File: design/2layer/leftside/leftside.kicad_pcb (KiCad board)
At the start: 2 copper layers, 142.6 x 96.2 mm, 215 parts, among them IC1 XCL240B333FR-G, IC3 nRF52833-QDAA-R7, IC4 TCA9537DGSR, IC5 XCL110A503KR-G, IC6 TPS22917LDBVT, IC7 SN74AHCT1G125DCKR, J1 USB_C_Receptacle_USB2.0_16P, J2 Battery+, J3 Battery-, J4 OLED_128x32, J6 Conn_01x04, J7 F32Q-1A7H1-11012, U1 BQ27441-G1, U2 BQ24072RGT, U3 USB6B1, U5 PEC11L-4015F-S0015, U6 PEC11L-4015F-S0015, Y1 ECS-320-8-37B2-JTY-TR

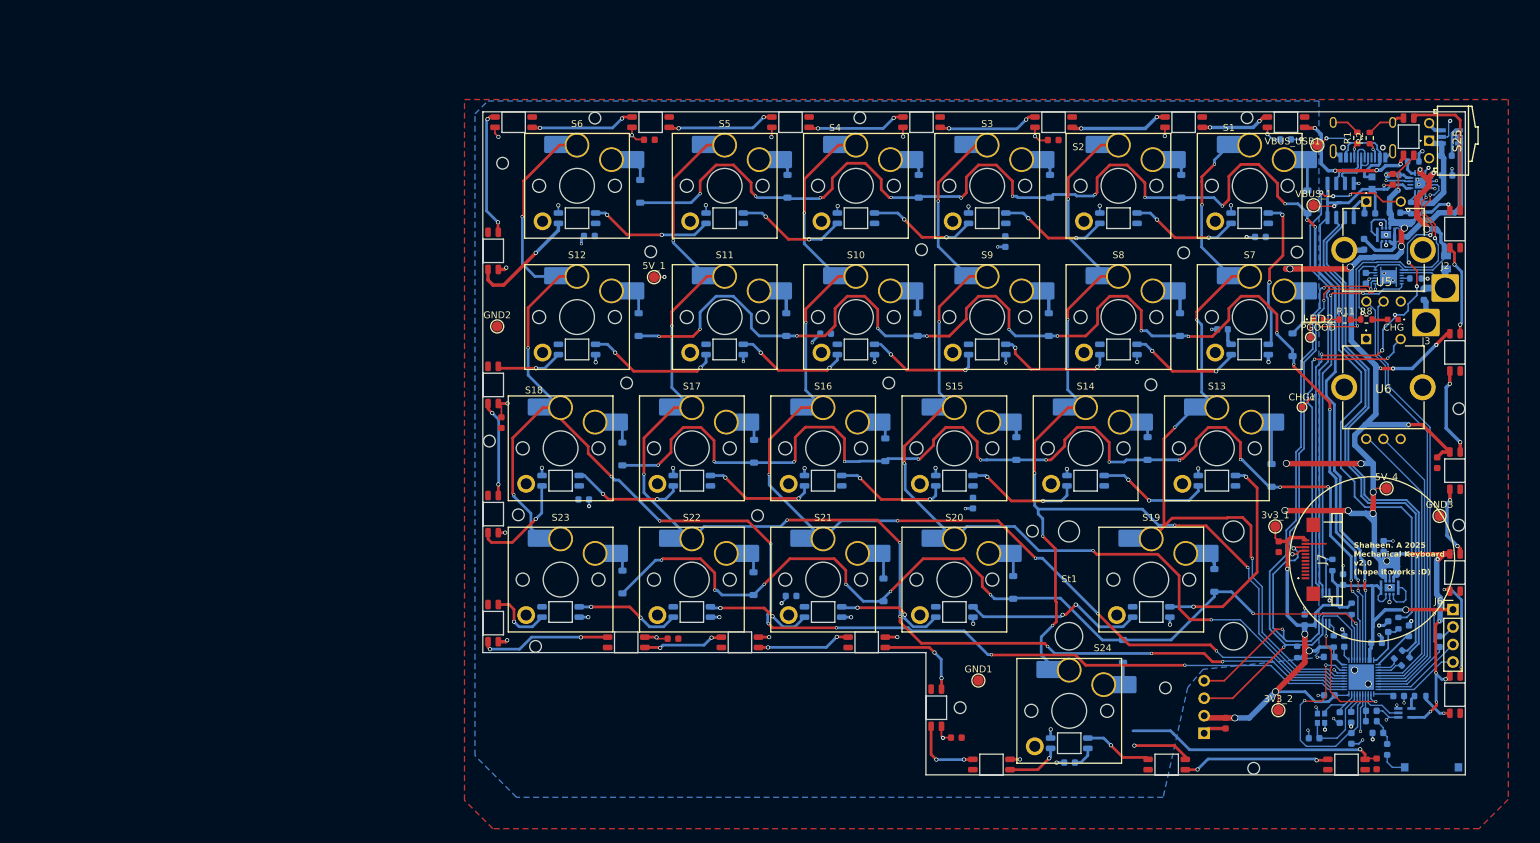
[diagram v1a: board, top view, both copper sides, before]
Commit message: begin better, more systematic 2 layer wiring
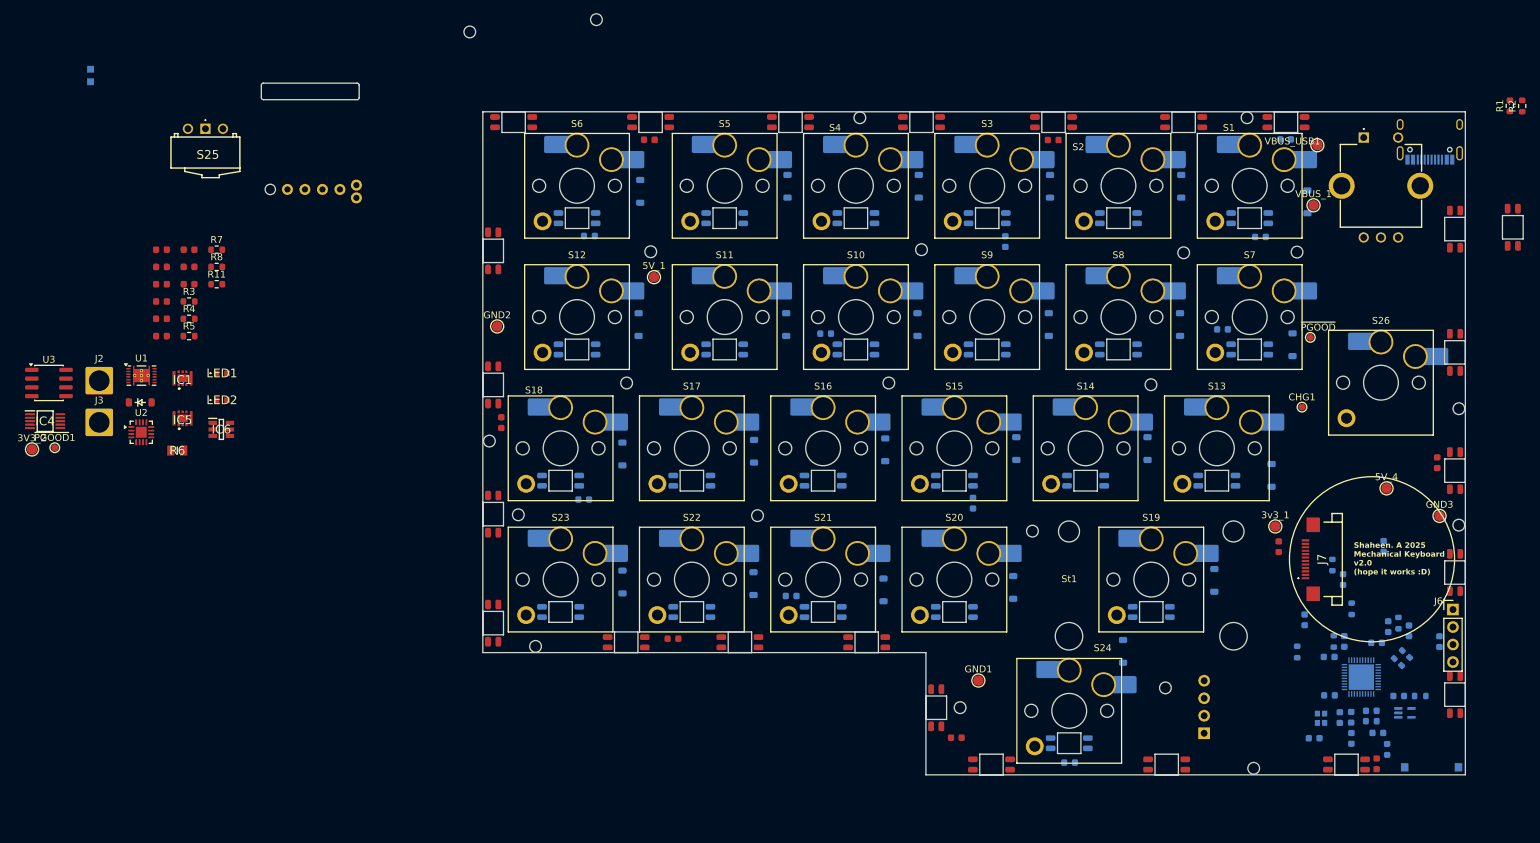
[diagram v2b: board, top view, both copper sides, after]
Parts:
- removed CHG: White LED KW_EEL, SamacSys_Parts:KWEELP41RUS1U13K6L3X4X5R18
- removed U6: PEC11L-4015F-S0015, SamacSys_Parts:PEC11L4015FS0015
- added Di25: Diode, ScottoKeebs_Components:Diode_SOD-123, F.Cu at (-31.7, 58.4)
- added EVQWGD1: ~, SamacSys_Parts:RollerEncoder_Panasonic_EVQWGD001, B.Cu at (-6.52, 21.9)
- added LED1: White LED KW_EEL, SamacSys:KWEELP41RUS1U13K6L3X4X5R18, F.Cu at (-19.8, 54.2)
- added S26: Keyswitch, ScottoKeebs_Hotswap:Hotswap_Choc_V1V2_Plated_1.00u, F.Cu at (148.4, 55.6)
- added ~{PGOOD}1: TestPoint, TestPoint:TestPoint_Pad_D1.0mm, F.Cu at (-44.1, 65.0)
- C10, C17, C22, C24, C25, C26, C48, R3, R4, R5, R7, U1, U2, U3: moved to F.Cu
- IC1, IC5: footprint SamacSys_Parts:XCL103D503CRG -> SamacSys:XCL103D503CRG; moved to F.Cu
- IC4: footprint SamacSys_Parts:SOP50P490X110-10N -> SamacSys:SOP50P490X110-10N; moved to F.Cu
- IC6: footprint SamacSys_Parts:SOT95P280X145-6N -> SamacSys:SOT95P280X145-6N; moved to F.Cu
- IC7: footprint SamacSys_Parts:SOT65P210X110-5N -> SamacSys:SOT65P210X110-5N
- J7: footprint SamacSys_Parts:F32Q1A7H111012 -> SamacSys:F32Q1A7H111012
- LED2: footprint SamacSys_Parts:KWEELP41RUS1U13K6L3X4X5R18 -> SamacSys:KWEELP41RUS1U13K6L3X4X5R18
- R6: footprint SamacSys_Parts:RESC2012X41N -> SamacSys:RESC2012X41N; moved to F.Cu
- Y1: footprint SamacSys_Parts:ECS320837B2JTYTR -> SamacSys:ECS320837B2JTYTR
- moved J2 195.8 mm to (-37.6, 55.3)
- moved J3 193.1 mm to (-37.6, 61.3)
- moved U3 189.3 mm to (-44.9, 55.6), turned to 0 degrees
- moved U2 189.1 mm to (-31.5, 62.8), turned to 0 degrees
- moved IC4 187.4 mm to (-45.5, 61.1), turned to 0 degrees
- moved C10 187.2 mm to (-28.6, 38.8)
- moved F1 186.6 mm to (-38.9, 11.0)
- moved R6 186.2 mm to (-26.3, 65.4), turned to 0 degrees
- moved 3V3_2 184.8 mm to (-47.4, 65.2)
- moved IC6 183.4 mm to (-19.9, 62.3)
- moved C48 183.3 mm to (-24.6, 41.3), turned to 0 degrees
- moved C17 183.2 mm to (-28.6, 41.3), turned to 0 degrees
- moved U1 181.6 mm to (-31.5, 54.5)
- moved C23 179.9 mm to (-28.6, 46.3), turned to 0 degrees
- moved R5 179.5 mm to (-24.6, 48.8), turned to 0 degrees
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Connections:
- Di1 pad 1: /Row 0 -> /Row 4
- Di11 pad 1: /Row 1 -> /Row 4
- Di20 pad 1: /Row 3 -> /Row 4
- Di4 pad 1: /Row 2 -> /Row 4
- IC3 pad 31: /Column 5 -> /Row 4
- S10 pad 1: /Column 3 -> /Column 2
- S11 pad 1: /Column 4 -> /Column 3
- S12 pad 1: /Column 5 -> /Column 4
- S13 pad 1: /Column 0 -> /Column 2
- S14 pad 1: /Column 1 -> /Column 0
- S15 pad 1: /Column 2 -> /Column 1
- S16 pad 1: /Column 3 -> /Column 2
- S17 pad 1: /Column 4 -> /Column 3
- S18 pad 1: /Column 5 -> /Column 4
- S19 pad 1: /Column 0 -> /Column 3
- S2 pad 1: /Column 1 -> /Column 0
- S20 pad 1: /Column 2 -> /Column 1
- S21 pad 1: /Column 3 -> /Column 2
- S22 pad 1: /Column 4 -> /Column 3
- S23 pad 1: /Column 5 -> /Column 4
- S24 pad 1: /Column 1 -> /Column 0
- S3 pad 1: /Column 2 -> /Column 1
- S4 pad 1: /Column 3 -> /Column 2
- S5 pad 1: /Column 4 -> /Column 3
- S6 pad 1: /Column 5 -> /Column 4
- S7 pad 1: /Column 0 -> /Column 1
- S8 pad 1: /Column 1 -> /Column 0
- S9 pad 1: /Column 2 -> /Column 1
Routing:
- net 5V: track 300.3 -> 0.00 mm, vias 43 -> 0
- net /Column 5: track 223.7 -> 0.00 mm, vias 10 -> 0
- net /Row 0: track 201.0 -> 0.00 mm, vias 14 -> 0
- net /Column 4: track 192.3 -> 0.00 mm, vias 9 -> 0
- net /Row 1: track 183.1 -> 0.00 mm, vias 14 -> 0
- net /Column 3: track 166.9 -> 0.00 mm, vias 7 -> 0
- net /Row 2: track 164.7 -> 0.00 mm, vias 14 -> 0
- net /Column 1: track 159.1 -> 0.00 mm, vias 7 -> 0
- net /Column 2: track 144.5 -> 0.00 mm, vias 5 -> 0
- net GND: track 138.7 -> 0.00 mm, vias 80 -> 0
- net /Row 3: track 137.3 -> 0.00 mm, vias 8 -> 0
- net 3V3: track 136.3 -> 0.00 mm, vias 7 -> 0
- net /Column 0: track 127.1 -> 0.00 mm, vias 5 -> 0
- net /SDA: track 102.3 -> 0.00 mm, vias 4 -> 0
- net /SCL: track 101.1 -> 0.00 mm, vias 4 -> 0
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- removed copper zone on B.Cu, net 5V
- removed copper zone on F.Cu, net GND
- removed copper zone on B.Cu, net Net-(IC5-1/VIN)
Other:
- board text added: "${REFERENCE}"

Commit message: V3 prep
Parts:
- removed the REF** at (117.1, 99.9)
- removed the REF** at (115.0, 55.9)
- removed the REF** at (38.9, 55.6)
- removed the REF** at (77.0, 55.6)
- removed the REF** at (23.2, 74.7)
- removed the REF** at (129.9, 111.5)
- removed the REF** at (119.8, 36.7)
- removed the REF** at (129.0, 17.1)
- removed the REF** at (159.7, 59.3)
- removed the REF** at (159.7, 76.2)
- removed the REF** at (19.0, 64.0)
- removed the REF** at (72.8, 17.1)
- removed the REF** at (57.9, 74.9)
- removed the REF** at (136.2, 36.6)
- removed the REF** at (81.7, 36.3)
- removed the REF** at (87.3, 102.7)
- removed the REF** at (16.1, 4.65)
- removed the REF** at (34.5, 2.87)
- removed the REF** at (25.7, 93.8)
- removed the REF** at (97.8, 77.1)
- removed ~{PGOOD}: TestPoint, TestPoint:TestPoint_Pad_D1.0mm
- added Di26: Diode, ScottoKeebs_Components:Diode_SOD-123, F.Cu at (-99.4, 68.4)
- added Di27: Diode, ScottoKeebs_Components:Diode_SOD-123, F.Cu at (-99.4, 71.8)
- added Di28: Diode, ScottoKeebs_Components:Diode_SOD-123, F.Cu at (-99.4, 75.1)
- added Di29: Diode, ScottoKeebs_Components:Diode_SOD-123, F.Cu at (-99.4, 78.5)
- added Di30: Diode, ScottoKeebs_Components:Diode_SOD-123, F.Cu at (-99.4, 81.8)
- added Di31: Diode, ScottoKeebs_Components:Diode_SOD-123, F.Cu at (-99.4, 85.2)
- added Di32: Diode, ScottoKeebs_Components:Diode_SOD-123, F.Cu at (-93.7, 68.4)
- added Di33: Diode, ScottoKeebs_Components:Diode_SOD-123, F.Cu at (-93.7, 71.8)
- added Di34: Diode, ScottoKeebs_Components:Diode_SOD-123, F.Cu at (-93.7, 75.1)
- added Di35: Diode, ScottoKeebs_Components:Diode_SOD-123, F.Cu at (-93.7, 78.5)
- added Di36: Diode, ScottoKeebs_Components:Diode_SOD-123, F.Cu at (-93.7, 81.8)
- added IC2: MCP23009-E_MG, LibraryLoader:QFN50P300X300X90-17N-D, F.Cu at (-88.2, 69.4)
- added IC8: TPS63051RMWT, LibraryLoader:QFN50P250X250X100-12N-D, F.Cu at (143.0, 97.4)
- added PC1: 10uF, ScottoKeebs_Components:Capacitor_0603, F.Cu at (-100.3, 42.9)
- added PC10: 100pF, ScottoKeebs_Components:Capacitor_0603, F.Cu at (-100.3, 57.9)
- added PC11: 100nF, ScottoKeebs_Components:Capacitor_0603, F.Cu at (-100.3, 60.5)
- added PC12: 1uF, ScottoKeebs_Components:Capacitor_0603, F.Cu at (-100.3, 63.0)
- added PC13: 1uF, ScottoKeebs_Components:Capacitor_0603, F.Cu at (-100.3, 65.5)
- added PC14: 47nF, ScottoKeebs_Components:Capacitor_0603, F.Cu at (-96.3, 42.9)
- added PC16: 4.7uF, ScottoKeebs_Components:Capacitor_0603, F.Cu at (-96.3, 45.4)
- added PC17: 4.7uF, ScottoKeebs_Components:Capacitor_0603, F.Cu at (-96.3, 47.9)
- added PC18: 100nF, ScottoKeebs_Components:Capacitor_0603, F.Cu at (-96.3, 50.4)
- added PC2: 4.7uF, ScottoKeebs_Components:Capacitor_0603, F.Cu at (-100.3, 45.4)
- added PC22: 470nF, ScottoKeebs_Components:Capacitor_0603, F.Cu at (-96.3, 52.9)
- added PC23: 4.7uF, ScottoKeebs_Components:Capacitor_0603, F.Cu at (-96.3, 55.4)
- added PC24: 4.7uF, ScottoKeebs_Components:Capacitor_0603, F.Cu at (-96.3, 57.9)
- added PC25: 10uF, ScottoKeebs_Components:Capacitor_0603, F.Cu at (-96.3, 60.5)
- added PC26: 10uF, ScottoKeebs_Components:Capacitor_0603, F.Cu at (-96.3, 63.0)
- added PC27: 10uF, ScottoKeebs_Components:Capacitor_0603, F.Cu at (-96.3, 65.5)
- added PC37: 100nF, ScottoKeebs_Components:Capacitor_0603, F.Cu at (-92.3, 42.9)
- added PC47: 10uF, ScottoKeebs_Components:Capacitor_0603, F.Cu at (-92.3, 45.4)
- added PC48: 4.7uF, ScottoKeebs_Components:Capacitor_0603, F.Cu at (-92.3, 47.9)
- added PC6: 4.7uF, ScottoKeebs_Components:Capacitor_0603, F.Cu at (-100.3, 47.9)
- added PC7: 100nF, ScottoKeebs_Components:Capacitor_0603, F.Cu at (-100.3, 50.4)
- added PC8: 820pF, ScottoKeebs_Components:Capacitor_0603, F.Cu at (-100.3, 52.9)
- added PC9: 4.7uF, ScottoKeebs_Components:Capacitor_0603, F.Cu at (-100.3, 55.4)
- added PG1: TestPoint, TestPoint:TestPoint_Pad_D1.5mm, F.Cu at (-84.2, 73.8)
- added PL3: 10uH, Inductor_SMD:L_0603_1608Metric, F.Cu at (-92.3, 50.4)
- added PL4: 15nH, Inductor_SMD:L_0603_1608Metric, F.Cu at (-92.3, 52.9)
- added PL5: 1.5uH, Inductor_SMD:L_0603_1608Metric, F.Cu at (-92.3, 55.4)
- added PR11: 270, Resistor_SMD:R_0603_1608Metric, F.Cu at (-92.3, 65.5)
- added PR17: 0, Resistor_SMD:R_0603_1608Metric, F.Cu at (-88.3, 42.9)
- added PR3: 1k8, Resistor_SMD:R_0603_1608Metric, F.Cu at (-92.3, 57.9)
- added PR4: 1k, Resistor_SMD:R_0603_1608Metric, F.Cu at (-92.3, 60.5)
- added PR8: 270, Resistor_SMD:R_0603_1608Metric, F.Cu at (-92.3, 63.0)
- added S27: Keyswitch, ScottoKeebs_Hotswap:Hotswap_Choc_V1V2_Plated_1.00u, F.Cu at (26.8, 24.4)
- added S28: Keyswitch, ScottoKeebs_Hotswap:Hotswap_Choc_V1V2_Plated_1.00u, F.Cu at (32.6, -57.2)
- added S29: Keyswitch, ScottoKeebs_Hotswap:Hotswap_Choc_V1V2_Plated_1.00u, F.Cu at (32.6, -39.9)
- added S30: Keyswitch, ScottoKeebs_Hotswap:Hotswap_Choc_V1V2_Plated_1.00u, F.Cu at (83.9, 24.4)
- added S31: Keyswitch, ScottoKeebs_Hotswap:Hotswap_Choc_V1V2_Plated_1.00u, F.Cu at (45.8, 24.4)
- added S32: Keyswitch, ScottoKeebs_Hotswap:Hotswap_Choc_V1V2_Plated_1.00u, F.Cu at (51.1, -57.2)
- added S33: Keyswitch, ScottoKeebs_Hotswap:Hotswap_Choc_V1V2_Plated_1.00u, F.Cu at (51.1, -39.9)
- added S34: Keyswitch, ScottoKeebs_Hotswap:Hotswap_Choc_V1V2_Plated_1.00u, F.Cu at (64.9, 24.4)
- added S35: Keyswitch, ScottoKeebs_Hotswap:Hotswap_Choc_V1V2_Plated_1.00u, F.Cu at (122.0, 24.4)
- added S36: Keyswitch, ScottoKeebs_Hotswap:Hotswap_Choc_V1V2_Plated_1.00u, F.Cu at (141.1, 24.4)
- added S37: Keyswitch, ScottoKeebs_Hotswap:Hotswap_Choc_V1V2_Plated_1.00u, F.Cu at (103.0, 24.4)
- added SC1: 12pF, ScottoKeebs_Components:Capacitor_0603, F.Cu at (-88.3, 45.4)
- added SC10: 10nF, ScottoKeebs_Components:Capacitor_0603, B.Cu at (144.1, 33.9)
- added SC19: 4.7uF, ScottoKeebs_Components:Capacitor_0603, F.Cu at (-88.3, 60.5)
- added SC2: 12pF, ScottoKeebs_Components:Capacitor_0603, F.Cu at (-88.3, 47.9)
- added SC3: 1pF, ScottoKeebs_Components:Capacitor_0603, F.Cu at (-88.3, 50.4)
- added SC4: 1.2pF, ScottoKeebs_Components:Capacitor_0603, F.Cu at (-88.3, 52.9)
- added SC5: 100nF, ScottoKeebs_Components:Capacitor_0603, F.Cu at (-88.3, 55.4)
- added SL1: 4.7nH, Inductor_SMD:L_0603_1608Metric, F.Cu at (-88.3, 63.0)
- added SL2: 2.2nH, Inductor_SMD:L_0603_1608Metric, F.Cu at (-88.3, 65.5)
- added SR1: 5k1, Resistor_SMD:R_0603_1608Metric, F.Cu at (-84.3, 42.9)
- added SR13: 4k7, Resistor_SMD:R_0603_1608Metric, F.Cu at (-84.3, 57.9)
- added SR14: 4k7, Resistor_SMD:R_0603_1608Metric, F.Cu at (-84.3, 60.5)
- added SR15: 22, Resistor_SMD:R_0603_1608Metric, F.Cu at (-84.3, 63.0)
- added SR16: 22, Resistor_SMD:R_0603_1608Metric, F.Cu at (-84.3, 65.5)
- added SR2: 5k1, Resistor_SMD:R_0603_1608Metric, F.Cu at (-84.3, 45.4)
- added SR3: 10k, Resistor_SMD:R_0603_1608Metric, F.Cu at (-84.3, 47.9)
- added SR4: 4k7, Resistor_SMD:R_0603_1608Metric, B.Cu at (147.1, 33.9)
- added SR5: 10k, Resistor_SMD:R_0603_1608Metric, F.Cu at (-84.3, 50.4)
- added SR7: 10k, Resistor_SMD:R_0603_1608Metric, F.Cu at (-84.3, 52.9)
- added SR9: 10k, Resistor_SMD:R_0603_1608Metric, F.Cu at (-84.3, 55.4)
- D15, D16, D17, D18, D19, D20, D21, D22, D23, D24, D25, D26, D29, D30, D31, D32, D33, D34, D35, D36, D37, D38, D39, D46, EVQWGD1, IC7, R10: moved to F.Cu
- IC6, R3, R4, R6, U2, U3: moved to B.Cu
- J2, J3: footprint Connector_Wire:SolderWire-2.5sqmm_1x01_D2.4mm_OD3.6mm -> Connector_Wire:SolderWire-0.75sqmm_1x01_D1.25mm_OD2.3mm
- moved GND3 226.9 mm to (-62.2, 15.6)
- moved 5V_4 221.9 mm to (-65.7, 15.6)
- moved 3v3_1 210.3 mm to (-69.3, 19.1)
- moved CHG1 209.1 mm to (-69.5, 26.0)
- moved U3 205.1 mm to (158.3, 27.5), turned to -90 degrees
- moved J3 202.7 mm to (162.9, 32.1)
- moved IC4 202.3 mm to (147.8, 120.6)
- moved VBUS_USB1 201.3 mm to (-62.2, 22.7)
- moved VBUS_1 201.0 mm to (-62.2, 19.1)
- moved IC5 198.9 mm to (171.5, 33.9)
- moved F1 193.3 mm to (153.9, 25.0)
- moved U1 187.2 mm to (154.4, 32.9), turned to 180 degrees
- moved C22 186.8 mm to (157.6, 29.5)
- moved LED2 184.8 mm to (162.5, 27.9), turned to 90 degrees
- moved U2 184.6 mm to (150.2, 30.3), turned to 180 degrees
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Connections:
- IC3 pad 14: /CCW2 -> /CW
- IC3 pad 15: /CW2 -> /CCW
- IC3 pad 16: /CCW -> /CCW2
- IC3 pad 17: /CW -> /LED
- IC3 pad 22: /INTA -> /CW2
- IC3 pad 23: /A -> /INTA
- IC3 pad 31: /Row 4 -> /Column 5
- IC3 pad 39: unconnected-(IC3-DCC-Pad39) -> Net-(IC3-DCC)
- IC3 pad 4: /Row 3 -> /CHG
- IC3 pad 5: /Row 2 -> /GPOUT
- IC3 pad 6: /Row 1 -> /NO
- IC3 pad 7: /Row 0 -> /NO2
- IC7 pad 2: /A -> /LED
- S25 pad 1: /OUT -> GND
- U1 pad 6: /BAT -> /SRP
- U2 pad 1: Net-(U2-TS) -> Net-(J5-Pin_1)
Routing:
- net Net-(IC6-ON): track 0.00 -> 118.4 mm
- net D-: track 0.00 -> 87.6 mm
- net D+: track 0.00 -> 87.5 mm
- net /SRP: track 0.00 -> 24.0 mm, vias 0 -> 1
- net Net-(IC3-SWDIO): track 0.00 -> 18.9 mm
- net /CCW: track 0.00 -> 18.4 mm, vias 0 -> 1
- net /CW: track 0.00 -> 18.4 mm, vias 0 -> 1
- net /CW2: track 0.00 -> 17.9 mm, vias 0 -> 1
- net Net-(IC3-SWDCLK): track 0.00 -> 17.1 mm
- net /~{PGOOD}: track 0.00 -> 15.7 mm, vias 0 -> 3
- net /CCW2: track 0.00 -> 15.6 mm, vias 0 -> 1
- net /BAT: track 0.00 -> 15.1 mm, vias 0 -> 2
- net Net-(D1-DOUT): track 0.00 -> 14.6 mm
- net /VBUS: track 0.00 -> 14.5 mm
- net /OUT: track 0.00 -> 8.67 mm
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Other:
- board size 142.6 x 96.2 mm -> 150 x 111.9 mm
- board text added: "Shaheen. A 2026 Mechanical Keyboard v3.0 (hope it works :D)"
- board text removed: "Shaheen. A 2025 Mechanical Keyboard v2.0 (hope it works :D)"

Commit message: Left side pre-stich
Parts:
- removed 3v3_1: TestPoint, TestPoint:TestPoint_Pad_D1.5mm
- removed C10: 100pF, ScottoKeebs_Components:Capacitor_0603
- removed C13, C25, C26: 10uF, ScottoKeebs_Components:Capacitor_0603
- removed C17, C23, C24, C47, C48, C9: 4.7uF, ScottoKeebs_Components:Capacitor_0603
- removed C18, C37, C7, C8: 100nF, ScottoKeebs_Components:Capacitor_0603
- removed C5: 1uF, ScottoKeebs_Components:Capacitor_0603
- removed Di31, Di32, Di33, Di35: Diode, ScottoKeebs_Components:Diode_SOD-123
- removed IC1: XCL240B333FR-G, SamacSys:XCL103D503CRG
- removed IC4: TCA9537DGSR, SamacSys:SOP50P490X110-10N
- removed the PC10 at (-100.3, 57.9)
- removed the PC13 at (-100.3, 65.5)
- removed the PC22 at (-96.3, 52.9)
- removed the PC8 at (-100.3, 52.9)
- removed the PR11 at (-92.3, 65.5)
- removed the PR3 at (-92.3, 57.9)
- removed the PR4 at (-92.3, 60.5)
- removed the PR8 at (-92.3, 63.0)
- removed R1, R2: 5k1, Resistor_SMD:R_0603_1608Metric
- removed R12, R5, R9: 10k, Resistor_SMD:R_0603_1608Metric
- removed R13, R14: 4k7, Resistor_SMD:R_0603_1608Metric
- removed R17: 0, Resistor_SMD:R_0603_1608Metric
- removed the S28 at (32.6, -57.2)
- removed the S29 at (32.6, -39.9)
- removed S32: Keyswitch, ScottoKeebs_Hotswap:Hotswap_Choc_V1V2_Plated_1.00u
- removed the S33 at (51.1, -39.9)
- removed the SC1 at (-88.3, 45.4)
- removed the SC2 at (-88.3, 47.9)
- removed the SC3 at (-88.3, 50.4)
- removed the SC4 at (-88.3, 52.9)
- removed the SL1 at (-88.3, 63.0)
- removed the SL2 at (-88.3, 65.5)
- removed the SR15 at (-84.3, 63.0)
- removed the SR16 at (-84.3, 65.5)
- removed the SR7 at (-84.3, 52.9)
- added D49: LED_SK6812MINI, ScottoKeebs_Components:LED_SK6812MINI, F.Cu at (148.2, 126.4)
- added D50: LED_SK6812MINI, ScottoKeebs_Components:LED_SK6812MINI, F.Cu at (133.3, 126.4)
- added D51: LED_SK6812MINI, ScottoKeebs_Components:LED_SK6812MINI, B.Cu at (83.9, 29.1)
- added D52: LED_SK6812MINI, ScottoKeebs_Components:LED_SK6812MINI, F.Cu at (74.4, 14.0)
- added D53: LED_SK6812MINI, ScottoKeebs_Components:LED_SK6812MINI, B.Cu at (131.6, 45.8)
- added D54: LED_SK6812MINI, ScottoKeebs_Components:LED_SK6812MINI, B.Cu at (131.6, 64.8)
- added D55: LED_SK6812MINI, ScottoKeebs_Components:LED_SK6812MINI, B.Cu at (126.8, 83.9)
- added D56: LED_SK6812MINI, ScottoKeebs_Components:LED_SK6812MINI, B.Cu at (117.3, 102.9)
- added D57: LED_SK6812MINI, ScottoKeebs_Components:LED_SK6812MINI, F.Cu at (119.0, 126.4)
- added D58: LED_SK6812MINI, ScottoKeebs_Components:LED_SK6812MINI, F.Cu at (100.6, 126.4)
- added D59: LED_SK6812MINI, ScottoKeebs_Components:LED_SK6812MINI, B.Cu at (79.2, 122.0)
- added D60: LED_SK6812MINI, ScottoKeebs_Components:LED_SK6812MINI, F.Cu at (86.3, 126.4)
- added D61: LED_SK6812MINI, ScottoKeebs_Components:LED_SK6812MINI, F.Cu at (55.4, 108.6)
- added D62: LED_SK6812MINI, ScottoKeebs_Components:LED_SK6812MINI, F.Cu at (68.8, 116.0)
- added D63: LED_SK6812MINI, ScottoKeebs_Components:LED_SK6812MINI, F.Cu at (72.0, 126.4)
- added J5: Conn_01x01, TestPoint:TestPoint_Pad_1.0x1.0mm, B.Cu at (155.6, 36.6)
- added J8: Conn_01x01, TestPoint:TestPoint_Pad_1.0x1.0mm, B.Cu at (154.9, 39.6)
- added PC3: 10uF, ScottoKeebs_Components:Capacitor_0603, B.Cu at (139.0, 95.1)
- C1, C2, C4: value 4.7uF -> 100nF
- C29, C30, C34, C38, C39, C41, C45, D13, D15, D17, D19, D21, D23, D26, D27, D28, D29, D30, D31, D32, D33, D34, D35, D38, D39, D4, D40, D41, D42, D43, D44, D45, D46, IC2, IC5, IC7, IC8, PC1, PC11, PC14, PC16, PC18, PC23, PC25, PC26, PC27, PC37, PC47, PC48, PC6, PC7, PC9, PL3, PL4, PL5, PR17, SC19, SC5, SR13, SR14, SR3, SR5, SR9, U1: moved to B.Cu
- Di1, Di10, Di11, Di12, Di13, Di14, Di15, Di16, Di17, Di18, Di19, Di2, Di20, Di21, Di22, Di23, Di24, Di3, Di4, Di5, Di6, Di7, Di8, Di9: moved to F.Cu
- PC22: renamed from C22; moved to B.Cu
- PR3: renamed from R3; value 540 -> 1k8
- PR4: renamed from R4; value 590 -> 1k
- SR10: renamed from R10; moved to B.Cu
- SR7: renamed from R7; moved to B.Cu
- VBUS_1, VBUS_USB1: footprint TestPoint:TestPoint_Pad_D1.5mm -> TestPoint:TestPoint_Pad_D1.0mm
- moved PC7 268.4 mm to (160.6, 113.7), turned to 45 degrees
- moved PC6 261.6 mm to (154.2, 108.7), turned to -135 degrees
- moved PC16 261.2 mm to (158.2, 104.2)
- moved PC24 255.2 mm to (156.4, 22.4), turned to 90 degrees
- moved Di36 254.0 mm to (153.0, 21.0), turned to 180 degrees
- moved Di34 253.5 mm to (159.3, 59.4), turned to -90 degrees
- moved PC2 252.7 mm to (151.9, 30.1), turned to -90 degrees
- moved PR17 252.1 mm to (156.7, 102.7)
- moved PC17 251.2 mm to (154.3, 30.1), turned to 180 degrees
- moved PC14 250.8 mm to (142.4, 119.7), turned to 180 degrees
- moved PC1 250.7 mm to (143.5, 101.3), turned to 90 degrees
- moved PC12 249.5 mm to (144.4, 111.6)
- moved SC19 249.2 mm to (156.0, 109.6), turned to -135 degrees
- moved PC23 247.6 mm to (149.3, 24.3)
- moved PC11 246.5 mm to (139.2, 118.5), turned to -90 degrees
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- renumbered C12 to PC10, C6 to PC13, C11 to PC8, R11 to PR11, R8 to PR8, S25 to S0, S23 to S1, S31 to S10, S21 to S11, S16 to S12, S10 to S13, S4 to S14, S34 to S15, S20 to S16, S15 to S17, S9 to S18, S3 to S19, S18 to S2, S30 to S20, S24 to S21, S14 to S22, S8 to S23, S2 to S24, S37 to S25, S19 to S26, S13 to S27, S7 to S28, S1 to S29, S12 to S3, S35 to S30, S26 to S33, S36 to S35, S6 to S4, S27 to S5, S22 to S6, S17 to S7, S11 to S8, S5 to S9, C14 to SC1, C19 to SC2, C16 to SC3, C15 to SC4, L1 to SL1, L2 to SL2, R15 to SR15, R16 to SR16
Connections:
- C1 pad 1: GND -> 5V
- C1 pad 2: 3V3 -> GND
- C2 pad 1: GND -> 5V
- C2 pad 2: Net-(IC3-VBUS) -> GND
- C3 pad 1: GND -> 5V
- C3 pad 2: Net-(IC3-DEC1) -> GND
- C4 pad 1: GND -> 5V
- C4 pad 2: Net-(IC3-DECUSB) -> GND
- D1 pad 2: Net-(D1-DOUT) -> unconnected-(D1-DOUT-Pad2)
- D11 pad 4: Net-(D10-DOUT) -> Net-(D11-DIN)
- D12 pad 2: Net-(D12-DOUT) -> Net-(D11-DIN)
- D12 pad 4: Net-(D11-DOUT) -> Net-(D12-DIN)
- D13 pad 2: Net-(D13-DOUT) -> Net-(D12-DIN)
- D13 pad 4: Net-(D12-DOUT) -> Net-(D13-DIN)
- D14 pad 2: Net-(D14-DOUT) -> Net-(D13-DIN)
- D14 pad 4: Net-(D13-DOUT) -> Net-(D14-DIN)
- D15 pad 2: Net-(D15-DOUT) -> Net-(D14-DIN)
- D15 pad 4: Net-(D14-DOUT) -> Net-(D15-DIN)
- D16 pad 2: Net-(D16-DOUT) -> Net-(D15-DIN)
- D16 pad 4: Net-(D15-DOUT) -> Net-(D16-DIN)
- D17 pad 2: Net-(D17-DOUT) -> Net-(D16-DIN)
- D17 pad 4: Net-(D16-DOUT) -> Net-(D17-DIN)
- D18 pad 2: Net-(D18-DOUT) -> Net-(D17-DIN)
- D18 pad 4: Net-(D17-DOUT) -> Net-(D18-DIN)
- D19 pad 4: Net-(D18-DOUT) -> Net-(D19-DIN)
- D2 pad 2: Net-(D2-DOUT) -> Net-(D1-DIN)
- D2 pad 4: Net-(D1-DOUT) -> Net-(D2-DIN)
- D20 pad 2: Net-(D20-DOUT) -> Net-(D19-DIN)
- D20 pad 4: Net-(D19-DOUT) -> Net-(D20-DIN)
- D21 pad 2: Net-(D21-DOUT) -> Net-(D20-DIN)
- D21 pad 4: Net-(D20-DOUT) -> Net-(D21-DIN)
- D22 pad 2: Net-(D22-DOUT) -> Net-(D21-DIN)
- D22 pad 4: Net-(D21-DOUT) -> Net-(D22-DIN)
- D23 pad 4: Net-(D22-DOUT) -> Net-(D23-DIN)
- D24 pad 2: Net-(D24-DOUT) -> Net-(D22-DIN)
- D24 pad 4: Net-(D23-DOUT) -> Net-(D24-DIN)
- D25 pad 2: Net-(D25-DOUT) -> Net-(D24-DIN)
- D25 pad 4: Net-(D24-DOUT) -> Net-(D23-DOUT)
- D26 pad 4: Net-(D25-DOUT) -> Net-(D26-DIN)
- D27 pad 2: Net-(D27-DOUT) -> Net-(D26-DIN)
- D27 pad 4: Net-(D26-DOUT) -> Net-(D27-DIN)
- D28 pad 2: Net-(D28-DOUT) -> Net-(D27-DIN)
- D28 pad 4: Net-(D27-DOUT) -> Net-(D28-DIN)
- D29 pad 2: Net-(D29-DOUT) -> Net-(D28-DIN)
- D29 pad 4: Net-(D28-DOUT) -> Net-(D29-DIN)
- D3 pad 2: Net-(D3-DOUT) -> Net-(D2-DIN)
- D3 pad 4: Net-(D2-DOUT) -> Net-(D3-DIN)
- D30 pad 2: Net-(D30-DOUT) -> Net-(D29-DIN)
- D30 pad 4: Net-(D29-DOUT) -> Net-(D30-DIN)
- D31 pad 4: Net-(D30-DOUT) -> Net-(D31-DIN)
- D32 pad 2: Net-(D32-DOUT) -> Net-(D31-DIN)
- D32 pad 4: Net-(D31-DOUT) -> Net-(D32-DIN)
- D33 pad 2: Net-(D33-DOUT) -> Net-(D32-DIN)
- D33 pad 4: Net-(D32-DOUT) -> Net-(D33-DIN)
- D34 pad 2: Net-(D34-DOUT) -> Net-(D33-DIN)
- D34 pad 4: Net-(D33-DOUT) -> Net-(D34-DIN)
- D35 pad 2: Net-(D35-DOUT) -> Net-(D34-DIN)
- D35 pad 4: Net-(D34-DOUT) -> Net-(D35-DIN)
- D36 pad 2: Net-(D36-DOUT) -> Net-(D35-DIN)
- D36 pad 4: Net-(D35-DOUT) -> Net-(D36-DIN)
- D37 pad 2: Net-(D37-DOUT) -> Net-(D36-DIN)
- D37 pad 4: Net-(D36-DOUT) -> Net-(D37-DIN)
- D38 pad 2: Net-(D38-DOUT) -> Net-(D37-DIN)
- D38 pad 4: Net-(D37-DOUT) -> Net-(D38-DIN)
- D39 pad 2: Net-(D39-DOUT) -> Net-(D38-DIN)
- D39 pad 4: Net-(D38-DOUT) -> Net-(D39-DIN)
- D4 pad 2: Net-(D4-DOUT) -> Net-(D3-DIN)
- D4 pad 4: Net-(D3-DOUT) -> Net-(D4-DIN)
- D40 pad 2: Net-(D40-DOUT) -> Net-(D39-DIN)
- D40 pad 4: Net-(D39-DOUT) -> Net-(D40-DIN)
- D41 pad 2: Net-(D41-DOUT) -> Net-(D40-DIN)
- D41 pad 4: Net-(D40-DOUT) -> Net-(D41-DIN)
- D42 pad 2: Net-(D42-DOUT) -> Net-(D41-DIN)
- D42 pad 4: Net-(D41-DOUT) -> Net-(D42-DIN)
- D43 pad 4: Net-(D42-DOUT) -> Net-(D43-DIN)
- D44 pad 2: Net-(D44-DOUT) -> Net-(D43-DIN)
- D44 pad 4: Net-(D43-DOUT) -> Net-(D44-DIN)
- D45 pad 2: Net-(D45-DOUT) -> Net-(D44-DIN)
- D45 pad 4: Net-(D44-DOUT) -> Net-(D45-DIN)
- D46 pad 2: Net-(D46-DOUT) -> Net-(D45-DIN)
- D46 pad 4: Net-(D45-DOUT) -> Net-(D10-DOUT)
- D47 pad 2: Net-(D47-DOUT) -> Net-(D23-DIN)
- D47 pad 4: Net-(D46-DOUT) -> Net-(D26-DOUT)
- D48 pad 2: unconnected-(D48-DOUT-Pad2) -> Net-(D4-DIN)
- D48 pad 4: Net-(D47-DOUT) -> Net-(D48-DIN)
- D5 pad 2: Net-(D5-DOUT) -> Net-(D48-DIN)
- D5 pad 4: Net-(D4-DOUT) -> Net-(D5-DIN)
- D6 pad 2: Net-(D6-DOUT) -> Net-(D5-DIN)
- D6 pad 4: Net-(D5-DOUT) -> Net-(D6-DIN)
- D7 pad 2: Net-(D7-DOUT) -> Net-(D6-DIN)
- D7 pad 4: Net-(D6-DOUT) -> Net-(D11-DOUT)
- D8 pad 2: Net-(D8-DOUT) -> Net-(D10-DIN)
- D8 pad 4: Net-(D7-DOUT) -> Net-(D8-DIN)
- D9 pad 2: Net-(D10-DIN) -> Net-(D8-DIN)
- D9 pad 4: Net-(D8-DOUT) -> Net-(D61-DOUT)
- Di1 pad 1: /Row 4 -> /Row 0
- Di10 pad 1: /Row 0 -> /Row 1
- Di11 pad 1: /Row 4 -> /Row 5
- Di12 pad 1: /Row 1 -> /Row 0
- Di13 pad 1: /Row 1 -> /Row 2
- Di14 pad 1: /Row 1 -> /Row 2
- Di15 pad 1: /Row 1 -> /Row 2
- Di16 pad 1: /Row 2 -> /Row 0
- Di17 pad 1: /Row 2 -> /Row 4
- Di18 pad 1: /Row 2 -> /Row 3
- Di19 pad 1: /Row 2 -> /Row 3
- Di2 pad 1: /Row 0 -> /Row 1
- Di20 pad 1: /Row 4 -> /Row 5
- Di22 pad 1: /Row 3 -> /Row 4
- Di23 pad 1: /Row 3 -> /Row 4
- Di24 pad 1: /Row 3 -> /Row 0
- Di25 pad 1: /Row 4 -> /Row 5
- Di26 pad 1: /Row 0 -> /Row 1
- Di27 pad 1: /Row 1 -> /Row 2
- Di28 pad 1: /Row 2 -> /Row 3
- Di29 pad 1: /Row 3 -> /Row 4
- Di3 pad 1: /Row 1 -> /Row 2
- Di30 pad 1: /Row 4 -> /Row 5
- Di34 pad 1: /Row 5 -> /Row 6
- Di36 pad 1: /Row 5 -> /Row 6
- Di4 pad 1: /Row 4 -> /Row 5
- Di5 pad 1: /Row 2 -> /Row 3
- Di6 pad 1: /Row 3 -> /Row 4
- Di8 pad 1: /Row 0 -> /Row 1
- Di9 pad 1: /Row 0 -> /Row 1
- IC2 pad 10: /Row 1 -> /Row 5
- IC2 pad 11: /Row 2 -> /Row 6
- IC2 pad 12: /Row 3 -> /Row 0
- IC2 pad 13: /Row 4 -> /Row 1
- IC2 pad 14: /Row 5 -> /Row 2
- IC2 pad 15: unconnected-(IC2-GP6-Pad15) -> /Row 3
- IC2 pad 16: unconnected-(IC2-GP7-Pad16) -> /Row 4
- IC2 pad 9: /Row 0 -> unconnected-(IC2-GP0-Pad9)
- IC3 pad 14: /CW -> /CCW
- IC3 pad 15: /CCW -> /CW
- IC3 pad 17: /LED -> /Column 2
- IC3 pad 23: /INTA -> unconnected-(IC3-P0.10-Pad23)
- IC3 pad 31: /Column 5 -> /LED
- IC3 pad 32: /Column 4 -> /INTA
- IC3 pad 33: /Column 3 -> /Column 0
- IC3 pad 34: /Column 2 -> /Column 3
- IC3 pad 36: /Column 0 -> /Column 4
- IC3 pad 4: /CHG -> /GPOUT
- IC3 pad 5: /GPOUT -> /NO2
- IC3 pad 6: /NO -> /CHG
- IC3 pad 7: /NO2 -> /NO
- S1 pad 1: /Column 4 -> /Column 0
- S1 pad 2: Net-(Di23-A) -> Net-(Di1-A)
- S10 pad 1: /Column 5 -> /Column 4
- S10 pad 2: Net-(Di30-A) -> Net-(Di26-A)
- S11 pad 1: /Column 2 -> /Column 0
- S11 pad 2: Net-(Di6-A) -> Net-(Di3-A)
- S12 pad 1: /Column 2 -> /Column 1
- S12 pad 2: Net-(Di18-A) -> Net-(Di13-A)
- S13 pad 2: Net-(Di13-A) -> Net-(Di14-A)
- S14 pad 1: /Column 2 -> /Column 3
- S14 pad 2: Net-(Di9-A) -> Net-(Di15-A)
- S15 pad 1: /Column 2 -> /Column 4
- S15 pad 2: Net-(Di33-A) -> Net-(Di27-A)
- S16 pad 1: /Column 1 -> /Column 0
- S17 pad 2: Net-(Di17-A) -> Net-(Di18-A)
- S18 pad 1: /Column 1 -> /Column 2
- S18 pad 2: Net-(Di3-A) -> Net-(Di5-A)
- S19 pad 1: /Column 1 -> /Column 3
- S19 pad 2: Net-(Di8-A) -> Net-(Di19-A)
- S2 pad 1: /Column 4 -> /Column 1
- S2 pad 2: Net-(Di19-A) -> Net-(Di7-A)
- S20 pad 1: /Column 5 -> /Column 4
- S20 pad 2: Net-(Di29-A) -> Net-(Di28-A)
- S21 pad 2: Net-(Di24-A) -> Net-(Di17-A)
- S22 pad 1: /Column 0 -> /Column 1
- S22 pad 2: Net-(Di16-A) -> Net-(Di6-A)
- S23 pad 1: /Column 0 -> /Column 2
- S23 pad 2: Net-(Di12-A) -> Net-(Di22-A)
- S24 pad 1: /Column 0 -> /Column 3
- S24 pad 2: Net-(Di7-A) -> Net-(Di23-A)
- S25 pad 1: /Column 5 -> /Column 4
- S25 pad 2: Net-(Di36-A) -> Net-(Di29-A)
- S26 pad 1: /Column 3 -> /Column 0
- S26 pad 2: Net-(Di20-A) -> Net-(Di11-A)
- S27 pad 1: /Column 2 -> /Column 1
- S28 pad 1: /Column 1 -> /Column 2
- S28 pad 2: Net-(Di11-A) -> Net-(Di20-A)
- S29 pad 1: /Column 0 -> /Column 3
- S29 pad 2: Net-(Di1-A) -> Net-(Di25-A)
- S3 pad 1: /Column 4 -> /Column 2
- S3 pad 2: Net-(Di15-A) -> Net-(Di12-A)
- S30 pad 1: /Column 3 -> /Column 4
- S30 pad 2: Net-(Di34-A) -> Net-(Di30-A)
- S33 pad 1: /Column 4 -> /Column 2
- S33 pad 2: Net-(Di25-A) -> Net-(Di34-A)
- S35 pad 2: Net-(Di35-A) -> Net-(Di36-A)
- S4 pad 1: /Column 4 -> /Column 3
- S4 pad 2: Net-(Di10-A) -> Net-(Di16-A)
- S5 pad 1: /Column 5 -> /Column 4
- S5 pad 2: Net-(Di26-A) -> Net-(Di24-A)
- S6 pad 1: /Column 3 -> /Column 0
- S6 pad 2: Net-(Di22-A) -> Net-(Di8-A)
- S7 pad 1: /Column 3 -> /Column 1
- S7 pad 2: Net-(Di5-A) -> Net-(Di9-A)
- S8 pad 1: /Column 3 -> /Column 2
- S8 pad 2: Net-(Di14-A) -> Net-(Di2-A)
- S9 pad 2: Net-(Di2-A) -> Net-(Di10-A)
- SR10 pad 2: Net-(D1-DIN) -> Net-(D49-DIN)
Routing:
- net /Column 4: track 0.00 -> 252.1 mm, vias 0 -> 16
- net /Column 3: track 0.00 -> 217.3 mm, vias 0 -> 10
- net /Column 2: track 0.00 -> 204.2 mm, vias 0 -> 5
- net /Row 0: track 0.00 -> 196.6 mm, vias 0 -> 17
- net /Row 1: track 0.00 -> 183.2 mm, vias 0 -> 17
- net /Column 0: track 0.00 -> 173.2 mm, vias 0 -> 9
- net /SDA: track 0.00 -> 169.5 mm, vias 0 -> 2
- net /SCL: track 0.00 -> 165.0 mm, vias 0 -> 4
- net /Row 2: track 0.00 -> 162.6 mm, vias 0 -> 15
- net /Column 1: track 0.00 -> 162.5 mm, vias 0 -> 5
- net 3V3: track 1.53 -> 163.2 mm, vias 1 -> 16
- net /Row 3: track 0.00 -> 156.5 mm, vias 0 -> 17
- net /Row 4: track 0.00 -> 155.7 mm, vias 0 -> 12
- net /Row 6: track 0.00 -> 137.7 mm, vias 0 -> 13
- net /Row 5: track 0.00 -> 115.3 mm, vias 0 -> 13
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- added copper zone on B.Cu, net 5V
- added copper zone on B.Cu, net GND
- added copper zone on F.Cu, net GND
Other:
- board size 150 x 111.9 mm -> 152.4 x 115.4 mm
- board text removed: "${REFERENCE}"
